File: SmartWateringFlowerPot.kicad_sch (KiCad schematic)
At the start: 32 parts, among them J1 USB-C 5V + USB2, J2 PUMP 5V, J3 MOISTURE, J4 RESERVOIR_SW, J5 FLOW optional, J6 UI OLED/ENC/LED, J7 DEBUG 3V3/GND/TX/RX/EN/BOOT, Q1 AO3400A, U1 ESP32-S3-WROOM-1-N8, U2 AP63203WU-7

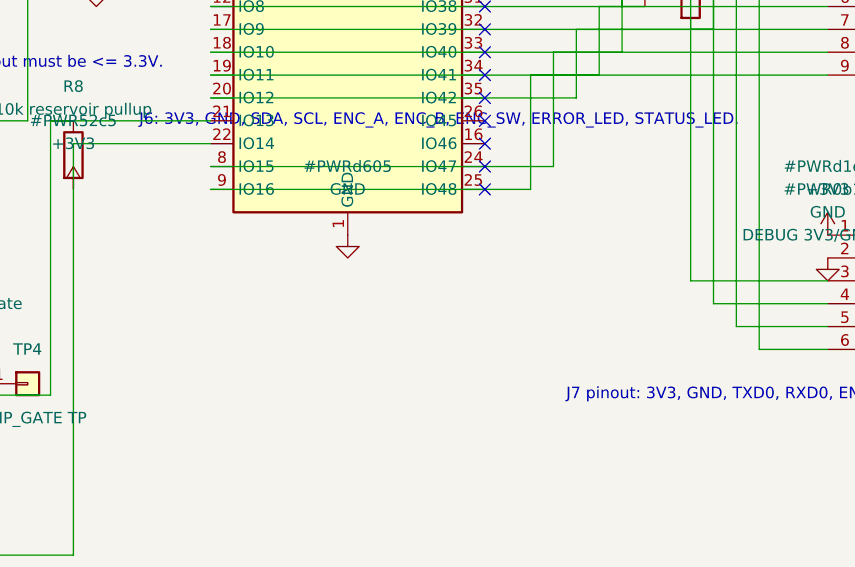
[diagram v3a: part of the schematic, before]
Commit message: Add Board B fab package and Board A hold report
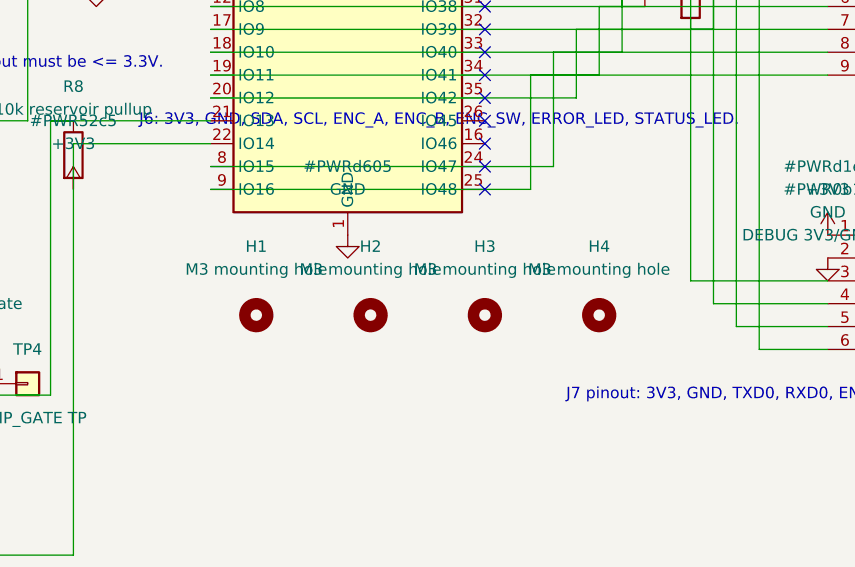
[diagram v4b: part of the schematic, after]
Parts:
- added H1, H2, H3, H4: M3 mounting hole, MountingHole:MountingHole_3.2mm_M3, symbol Mechanical:MountingHole
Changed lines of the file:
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@@
+		)
+	)
+	(symbol
+		(lib_id "Mechanical:MountingHole")
+		(at 142.24 128.27 0)
+		(unit 1)
+		(exclude_from_sim no)
+		(in_bom no)
+		(on_board yes)
+		(dnp no)
+		(property "Reference" "H1"
+			(at 142.24 120.65 0)
+			(effects
+				(font
+					(size 1.27 1.27)
+				)
+			)
+		)
+		(property "Value" "M3 mounting hole"
+			(at 142.24 123.19 0)
+			(effects
+				(font
+					(size 1.27 1.27)
+				)
+			)
+		)
+		(property "Footprint" "MountingHole:MountingHole_3.2mm_M3"
+			(at 142.24 128.27 0)
+			(effects
+				(font
+					(size 1.27 1.27)
+				)
+				(hide yes)
+			)
+		)
+		(property "Datasheet" "~"
+			(at 142.24 128.27 0)
+			(effects
+				(font
+					(size 1.27 1.27)
+				)
+				(hide yes)
+			)
+		)
+		(instances
+			(project ""
+				(path "/f5104368-02d7-408f-bed6-2d0faa538216"
+					(reference "H1")
+					(unit 1)
+				)
+			)
+		)
+	)
+	(symbol
+		(lib_id "Mechanical:MountingHole")
+		(at 154.94 128.27 0)
+		(unit 1)
+		(exclude_from_sim no)
+		(in_bom no)
+		(on_board yes)
+		(dnp no)
+		(property "Reference" "H2"
+			(at 154.94 120.65 0)
+			(effects
+				(font
+					(size 1.27 1.27)
+				)
+			)
+		)
+		(property "Value" "M3 mounting hole"
+			(at 154.94 123.19 0)
+			(effects
+				(font
+					(size 1.27 1.27)
+				)
+			)
+		)
+		(property "Footprint" "MountingHole:MountingHole_3.2mm_M3"
+			(at 154.94 128.27 0)
+			(effects
+				(font
+					(size 1.27 1.27)
+				)
+				(hide yes)
+			)
+		)
+		(property "Datasheet" "~"
+			(at 154.94 128.27 0)
+			(effects
+				(font
+					(size 1.27 1.27)
+				)
+				(hide yes)
+			)
+		)
+		(instances
+			(project ""
+				(path "/f5104368-02d7-408f-bed6-2d0faa538216"
+					(reference "H2")
+					(unit 1)
+				)
+			)
+		)
+	)
+	(symbol
+		(lib_id "Mechanical:MountingHole")
+		(at 167.64 128.27 0)
+		(unit 1)
+		(exclude_from_sim no)
+		(in_bom no)
+		(on_board yes)
+		(dnp no)
+		(property "Reference" "H3"
+			(at 167.64 120.65 0)
+			(effects
+				(font
+					(size 1.27 1.27)
+				)
+			)
+		)
+		(property "Value" "M3 mounting hole"
+			(at 167.64 123.19 0)
+			(effects
+				(font
+					(size 1.27 1.27)
+				)
+			)
+		)
+		(property "Footprint" "MountingHole:MountingHole_3.2mm_M3"
+			(at 167.64 128.27 0)
+			(effects
+				(font
+					(size 1.27 1.27)
+				)
+				(hide yes)
+			)
+		)
+		(property "Datasheet" "~"
+			(at 167.64 128.27 0)
+			(effects
+				(font
+					(size 1.27 1.27)
+				)
+				(hide yes)
+			)
+		)
+		(instances
+			(project ""
+				(path "/f5104368-02d7-408f-bed6-2d0faa538216"
+					(reference "H3")
+					(unit 1)
+				)
+			)
+		)
+	)
+	(symbol
+		(lib_id "Mechanical:MountingHole")
+		(at 180.34 128.27 0)
+		(unit 1)
+		(exclude_from_sim no)
+		(in_bom no)
+		(on_board yes)
+		(dnp no)
+		(property "Reference" "H4"
+			(at 180.34 120.65 0)
+			(effects
+				(font
+					(size 1.27 1.27)
+				)
+			)
+		)
+		(property "Value" "M3 mounting hole"
+			(at 180.34 123.19 0)
+			(effects
+				(font
+					(size 1.27 1.27)
+				)
+			)
+		)
+		(property "Footprint" "MountingHole:MountingHole_3.2mm_M3"
+			(at 180.34 128.27 0)
+			(effects
+				(font
+					(size 1.27 1.27)
+				)
+				(hide yes)
+			)
+		)
+		(property "Datasheet" "~"
+			(at 180.34 128.27 0)
+			(effects
+				(font
+					(size 1.27 1.27)
+				)
+				(hide yes)
+			)
+		)
+		(instances
+			(project ""
+				(path "/f5104368-02d7-408f-bed6-2d0faa538216"
+					(reference "H4")
+					(unit 1)
+				)
+			)
 		)
 	)

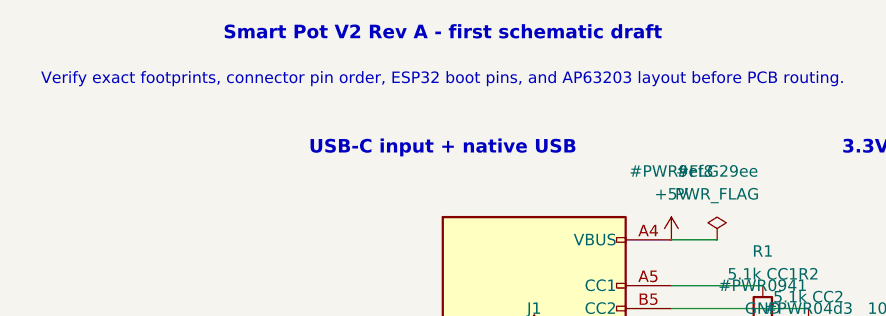
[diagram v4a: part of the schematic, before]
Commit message: Rebrand order package and add five-unit BOM
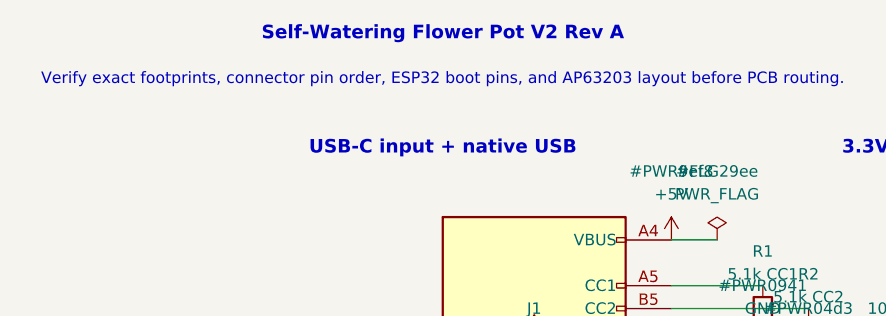
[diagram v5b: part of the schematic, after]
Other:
- note added: "Self-Watering Flower Pot V2 Rev A"
- note removed: "Smart Pot V2 Rev A - first schematic draft"
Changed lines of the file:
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@@
 	(generator_version "9.0")
 	(paper "A4")
-	(text "Smart Pot V2 Rev A - first schematic draft"
+	(text "Self-Watering Flower Pot V2 Rev A"
 		(at 20.32 12.7 0)
 		(effects

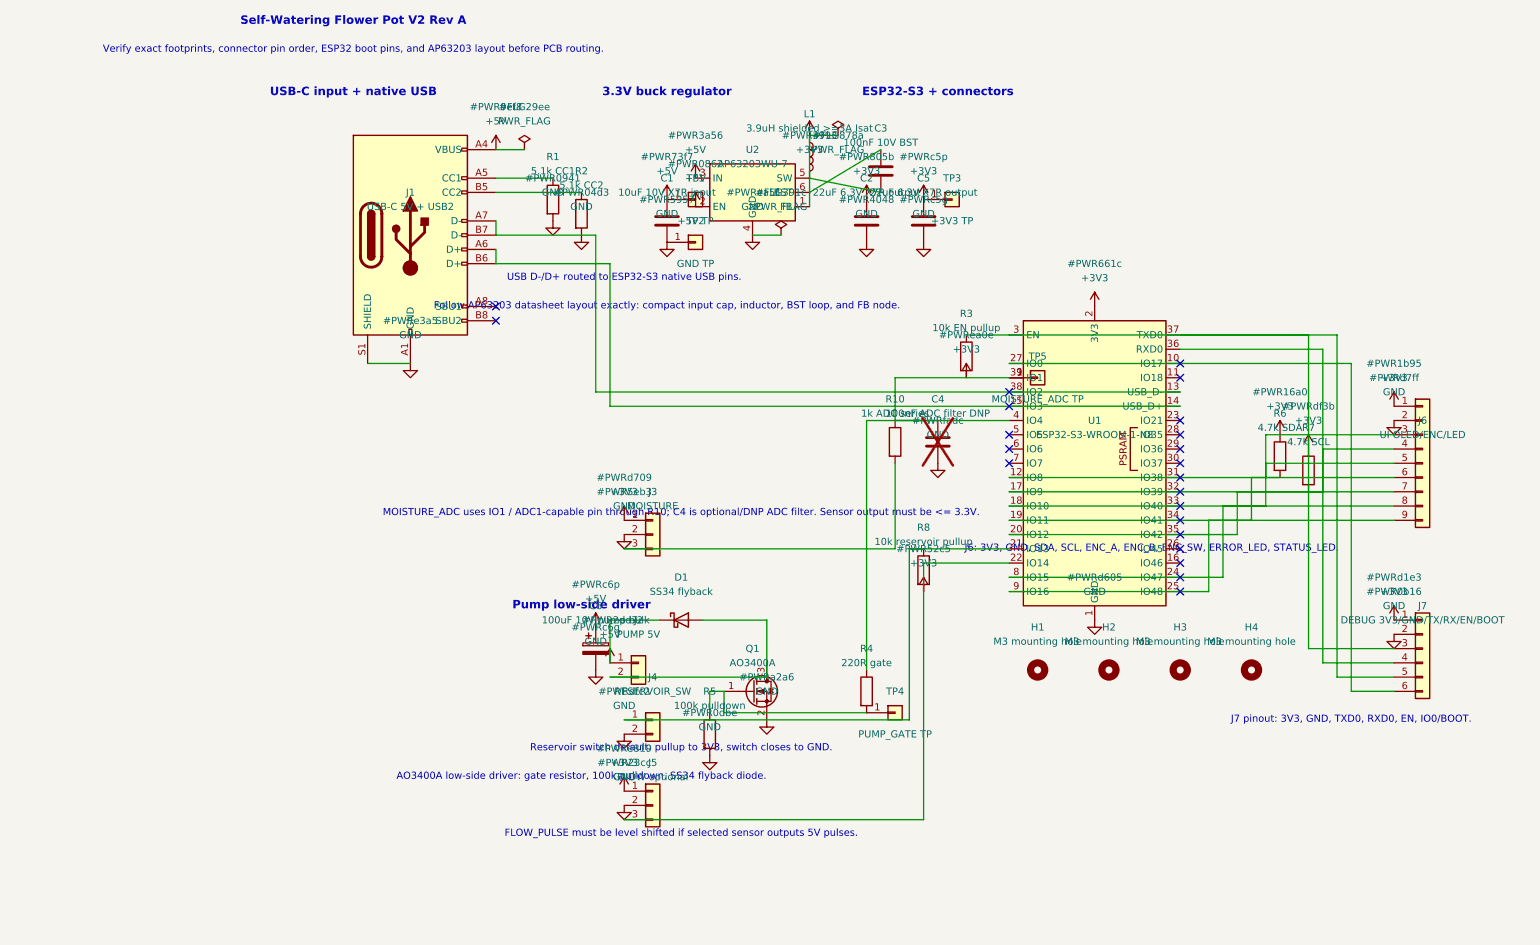
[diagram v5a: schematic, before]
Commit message: Implement board-a-only cost-down redesign
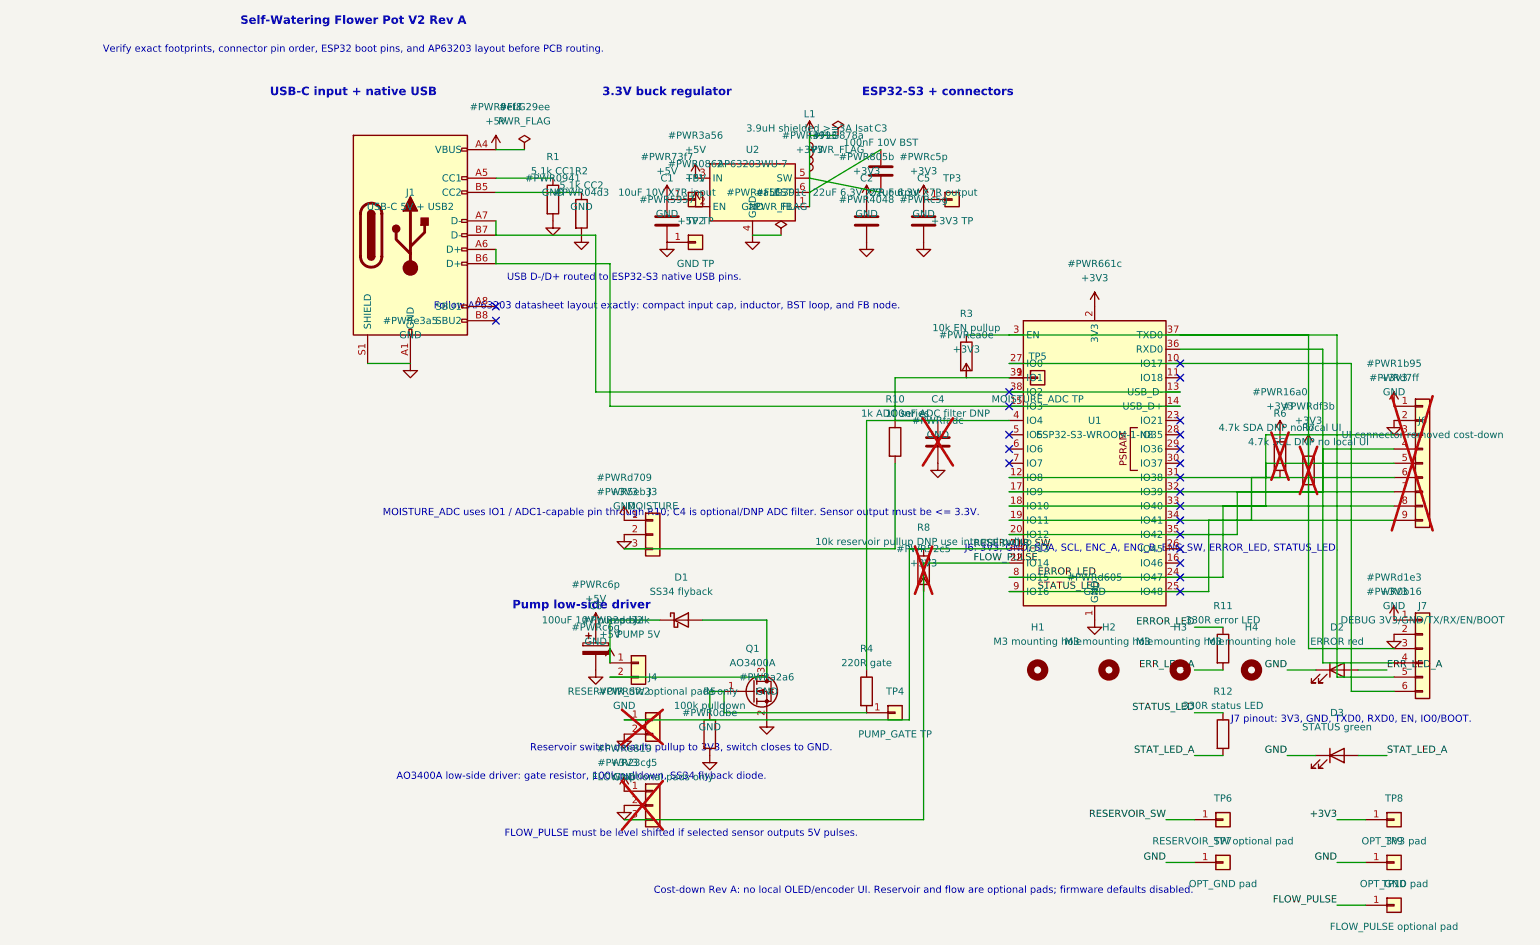
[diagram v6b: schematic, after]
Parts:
- added D2: ERROR red, LED_SMD:LED_0805_2012Metric, symbol Device:LED
- added D3: STATUS green, LED_SMD:LED_0805_2012Metric, symbol Device:LED
- added R11: 330R error LED, Resistor_SMD:R_0805_2012Metric, symbol Device:R
- added R12: 330R status LED, Resistor_SMD:R_0805_2012Metric, symbol Device:R
- added TP10: FLOW_PULSE optional pad, TestPoint:TestPoint_Pad_D1.5mm, symbol Connector_Generic:Conn_01x01
- added TP6: RESERVOIR_SW optional pad, TestPoint:TestPoint_Pad_D1.5mm, symbol Connector_Generic:Conn_01x01
- added TP7, TP9: OPT_GND pad, TestPoint:TestPoint_Pad_D1.5mm, symbol Connector_Generic:Conn_01x01
- added TP8: OPT_3V3 pad, TestPoint:TestPoint_Pad_D1.5mm, symbol Connector_Generic:Conn_01x01
- J4: value RESERVOIR_SW -> RESERVOIR_SW optional pads only; now not fitted; now left out of the parts list
- J5: value FLOW optional -> FLOW optional pads only; now not fitted; now left out of the parts list
- J6: value UI OLED/ENC/LED -> UI connector removed cost-down; now not fitted; now left out of the parts list
- R6: value 4.7k SDA -> 4.7k SDA DNP no local UI; now not fitted; now left out of the parts list
- R7: value 4.7k SCL -> 4.7k SCL DNP no local UI; now not fitted; now left out of the parts list
- R8: value 10k reservoir pullup -> 10k reservoir pullup DNP use internal pullup; now not fitted; now left out of the parts list
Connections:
- net +3V3: now also TP8.1 (Pin_1)
- net GND: now also D2.1 (K), D3.1 (K), TP7.1 (Pin_1), TP9.1 (Pin_1)
- net RESERVOIR_SW: now reaches J4.1 (Pin_1), R8.1, U1.21 (IO13)
- net RESERVOIR_SW: now also TP6.1 (Pin_1)
- net FLOW_PULSE: now reaches J5.3 (Pin_3), U1.22 (IO14)
- net FLOW_PULSE: now also TP10.1 (Pin_1)
- net ERROR_LED: now reaches J6.3 (Pin_3), J6.5 (Pin_5), J6.6 (Pin_6), J6.8 (Pin_8), J6.9 (Pin_9), R6.2, U1.12 (IO8), U1.18 (IO10), U1.19 (IO11), U1.8 (IO15), U1.9 (IO16)
- net ERROR_LED: now also R11.1, R12.1
- new net ERR_LED_A: D2.2 (A), R11.2
- new net STAT_LED_A: D3.2 (A), R12.2
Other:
- note added: "Cost-down Rev A: no local OLED/encoder UI. Reservoir and flow are optional pads; firmware defaults disabled."
